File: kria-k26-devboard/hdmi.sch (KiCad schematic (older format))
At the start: 1 part

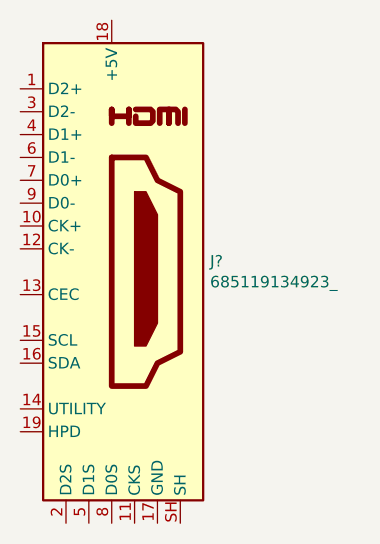
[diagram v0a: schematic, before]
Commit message: First sketches of POE part of supply
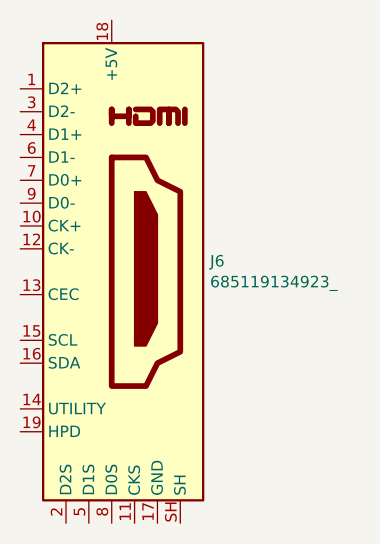
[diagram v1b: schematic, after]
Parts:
- gave numbers to parts that had none: 1
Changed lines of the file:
@@
 $EndDescr
 $Comp
-L antmicroUSBDVIHDMIConnectors:685119134923_ J?
+L antmicroUSBDVIHDMIConnectors:685119134923_ J6
 U 1 1 63CAF304
 P 5600 3750
-F 0 "J?" H 6030 3796 50  0000 L CNN
+F 0 "J6" H 6030 3796 50  0000 L CNN
 F 1 "685119134923_" H 6030 3705 50  0000 L CNN
 F 2 "antmicro-footprints:HDMI_A_Female_685119134923" H 5800 3950 60  0001 L CNN

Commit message: Locklib+ added layer table
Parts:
- J6: footprint antmicro-footprints:HDMI_A_Female_685119134923 -> kria-k26-devboard-footprints:HDMI_A_Female_685119134923; symbol antmicroUSBDVIHDMIConnectors:685119134923_ -> kria-k26-devboard:685119134923_
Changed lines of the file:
@@
 $EndDescr
 $Comp
-L antmicroUSBDVIHDMIConnectors:685119134923_ J6
+L kria-k26-devboard:685119134923_ J6
 U 1 1 63CAF304
 P 5600 3750
 F 0 "J6" H 6030 3796 50  0000 L CNN
 F 1 "685119134923_" H 6030 3705 50  0000 L CNN
-F 2 "antmicro-footprints:HDMI_A_Female_685119134923" H 5800 3950 60  0001 L CNN
+F 2 "kria-k26-devboard-footprints:HDMI_A_Female_685119134923" H 5800 3950 60  0001 L CNN
 F 3 "https://katalog.we-online.de/em/datasheet/685119134923.pdf" H 5625 3750 50  0001 C CNN
 	1    5600 3750
